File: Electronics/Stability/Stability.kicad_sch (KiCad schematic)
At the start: 0 parts

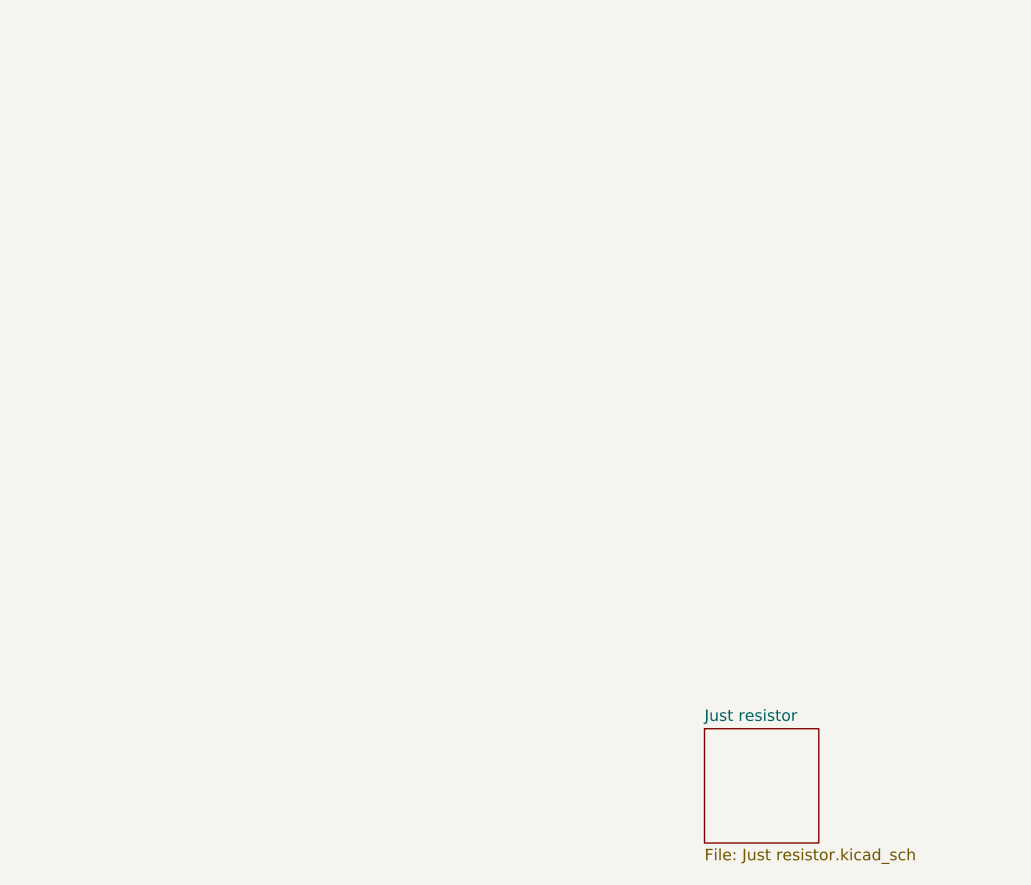
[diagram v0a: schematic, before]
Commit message: Create resistor + capacitor simulation
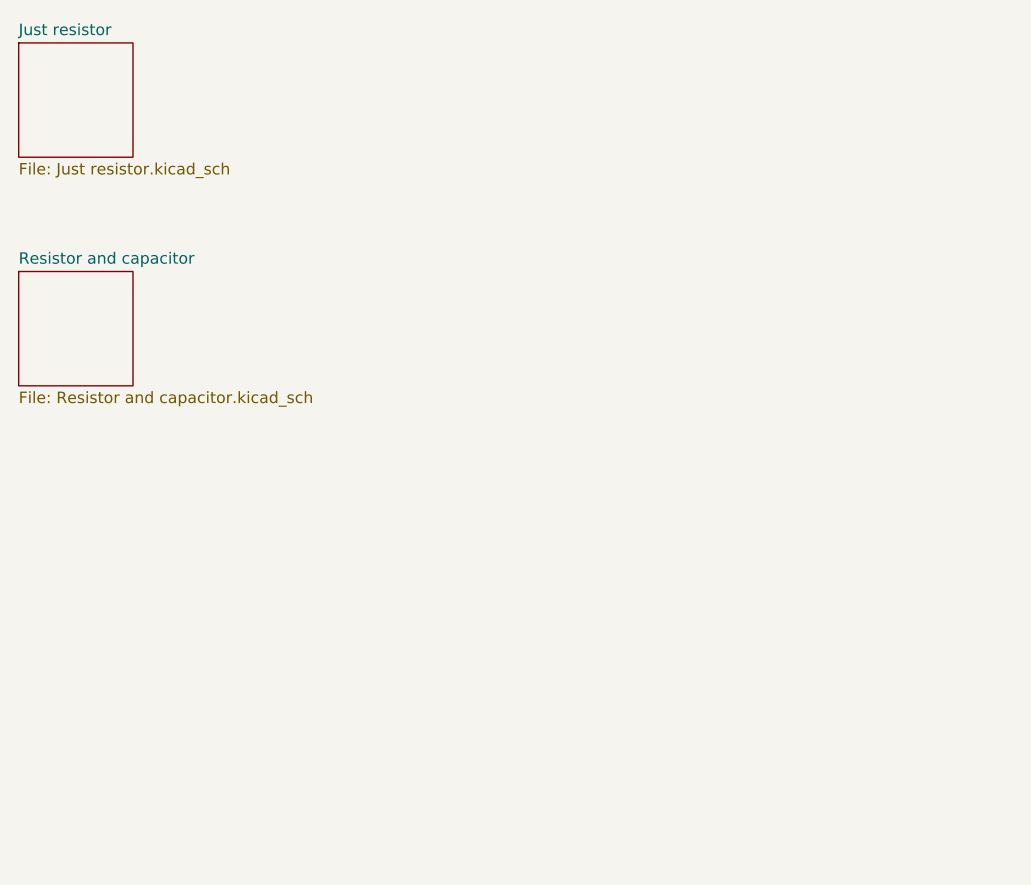
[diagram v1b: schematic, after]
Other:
- added sheet Resistor and capacitor (Resistor and capacitor.kicad_sch)
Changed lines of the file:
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@@
 	(paper "A4")
 	(sheet
-		(at 101.6 101.6)
+		(at 25.4 25.4)
 		(size 12.7 12.7)
-		(exclude_from_sim no)
+		(exclude_from_sim yes)
 		(in_bom yes)
 		(on_board yes)
@@
 		)
 		(property "Sheetname" "Just resistor"
-			(at 101.6 100.8884 0)
+			(at 25.4 24.6884 0)
 			(show_name no)
 			(do_not_autoplace no)
@@
 		)
 		(property "Sheetfile" "Just resistor.kicad_sch"
-			(at 101.6 114.8846 0)
+			(at 25.4 38.6846 0)
 			(show_name no)
 			(do_not_autoplace no)
@@
 				)
 			)
+		)
+	)
+	(sheet
+		(at 25.4 50.8)
+		(size 12.7 12.7)
+		(exclude_from_sim no)
+		(in_bom yes)
+		(on_board yes)
+		(dnp no)
+		(fields_autoplaced yes)
+		(stroke
+			(width 0.1524)
+			(type solid)
+		)
+		(fill
+			(color 0 0 0 0)
+		)
+		(property "Sheetname" "Resistor and capacitor"
+			(at 25.4 50.0884 0)
+			(show_name no)
+			(do_not_autoplace no)
+			(effects
+				(font
+					(size 1.27 1.27)
+				)
+				(justify left bottom)
+			)
+		)
+		(property "Sheetfile" "Resistor and capacitor.kicad_sch"
+			(at 25.4 64.0846 0)
+			(show_name no)
+			(do_not_autoplace no)
+			(effects
+				(font
+					(size 1.27 1.27)
+				)
+				(justify left top)
+			)
+		)
+		(instances
+			(project "Stability"
+				(path "/01684154-c57f-44f9-be7e-34aae891c09d"
+					(page "3")
+				)
+			)

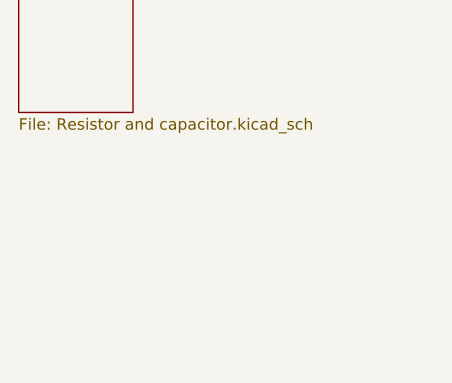
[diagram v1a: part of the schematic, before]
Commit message: Create stability compensation simulation
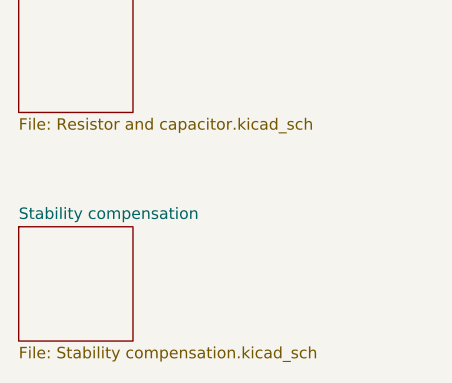
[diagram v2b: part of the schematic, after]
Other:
- added sheet Stability compensation (Stability compensation.kicad_sch)
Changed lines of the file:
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@@
+	)
+	(sheet
+		(at 25.4 76.2)
+		(size 12.7 12.7)
+		(exclude_from_sim no)
+		(in_bom yes)
+		(on_board yes)
+		(dnp no)
+		(fields_autoplaced yes)
+		(stroke
+			(width 0.1524)
+			(type solid)
+		)
+		(fill
+			(color 0 0 0 0)
+		)
+		(property "Sheetname" "Stability compensation"
+			(at 25.4 75.4884 0)
+			(show_name no)
+			(do_not_autoplace no)
+			(effects
+				(font
+					(size 1.27 1.27)
+				)
+				(justify left bottom)
+			)
+		)
+		(property "Sheetfile" "Stability compensation.kicad_sch"
+			(at 25.4 89.4846 0)
+			(show_name no)
+			(do_not_autoplace no)
+			(effects
+				(font
+					(size 1.27 1.27)
+				)
+				(justify left top)
+			)
+		)
+		(instances
+			(project "Stability"
+				(path "/01684154-c57f-44f9-be7e-34aae891c09d"
+					(page "4")
+				)
+			)
+		)
 	)
 	(sheet
 		(at 25.4 50.8)
 		(size 12.7 12.7)
-		(exclude_from_sim no)
+		(exclude_from_sim yes)
 		(in_bom yes)
 		(on_board yes)

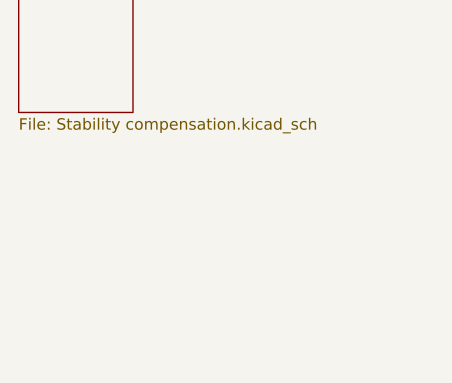
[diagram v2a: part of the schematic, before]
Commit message: Add OPA858 stability simulation
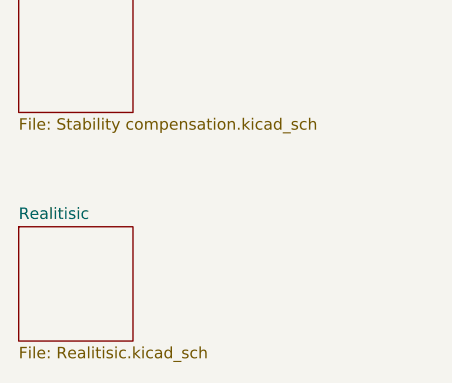
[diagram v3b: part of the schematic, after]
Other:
- added sheet Realitisic (Realitisic.kicad_sch)
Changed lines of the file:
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@@
+	)
+	(sheet
+		(at 25.4 101.6)
+		(size 12.7 12.7)
+		(exclude_from_sim yes)
+		(in_bom yes)
+		(on_board yes)
+		(dnp no)
+		(fields_autoplaced yes)
+		(stroke
+			(width 0.1524)
+			(type solid)
+		)
+		(fill
+			(color 0 0 0 0)
+		)
+		(property "Sheetname" "Realitisic"
+			(at 25.4 100.8884 0)
+			(show_name no)
+			(do_not_autoplace no)
+			(effects
+				(font
+					(size 1.27 1.27)
+				)
+				(justify left bottom)
+			)
+		)
+		(property "Sheetfile" "Realitisic.kicad_sch"
+			(at 25.4 114.8846 0)
+			(show_name no)
+			(do_not_autoplace no)
+			(effects
+				(font
+					(size 1.27 1.27)
+				)
+				(justify left top)
+			)
+		)
+		(property "Field2" ""
+			(at 25.4 101.6 0)
+			(hide yes)
+			(show_name no)
+			(do_not_autoplace no)
+			(effects
+				(font
+					(size 1.27 1.27)
+				)
+			)
+		)
+		(instances
+			(project "Stability"
+				(path "/01684154-c57f-44f9-be7e-34aae891c09d"
+					(page "5")
+				)
+			)
+		)
 	)
 	(sheet
 		(at 25.4 76.2)
 		(size 12.7 12.7)
-		(exclude_from_sim no)
+		(exclude_from_sim yes)
 		(in_bom yes)
 		(on_board yes)
@@
 		(at 25.4 50.8)
 		(size 12.7 12.7)
-		(exclude_from_sim yes)
+		(exclude_from_sim no)
 		(in_bom yes)
 		(on_board yes)
